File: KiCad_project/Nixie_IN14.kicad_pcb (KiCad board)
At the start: 2 copper layers, 319.8 x 69.7 mm, 65 parts, among them J1 Conn_01x10_Pin, J2 Conn_01x07_Pin, J3 Conn_01x07_Pin, J4 Conn_01x10_Pin, J5 Conn_01x07_Pin, J6 Conn_01x07_Pin, J7 USB_C_Receptacle_PowerOnly_6P, Q1 IRF540N, Q2 MMBTA42, U1 BME280_module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

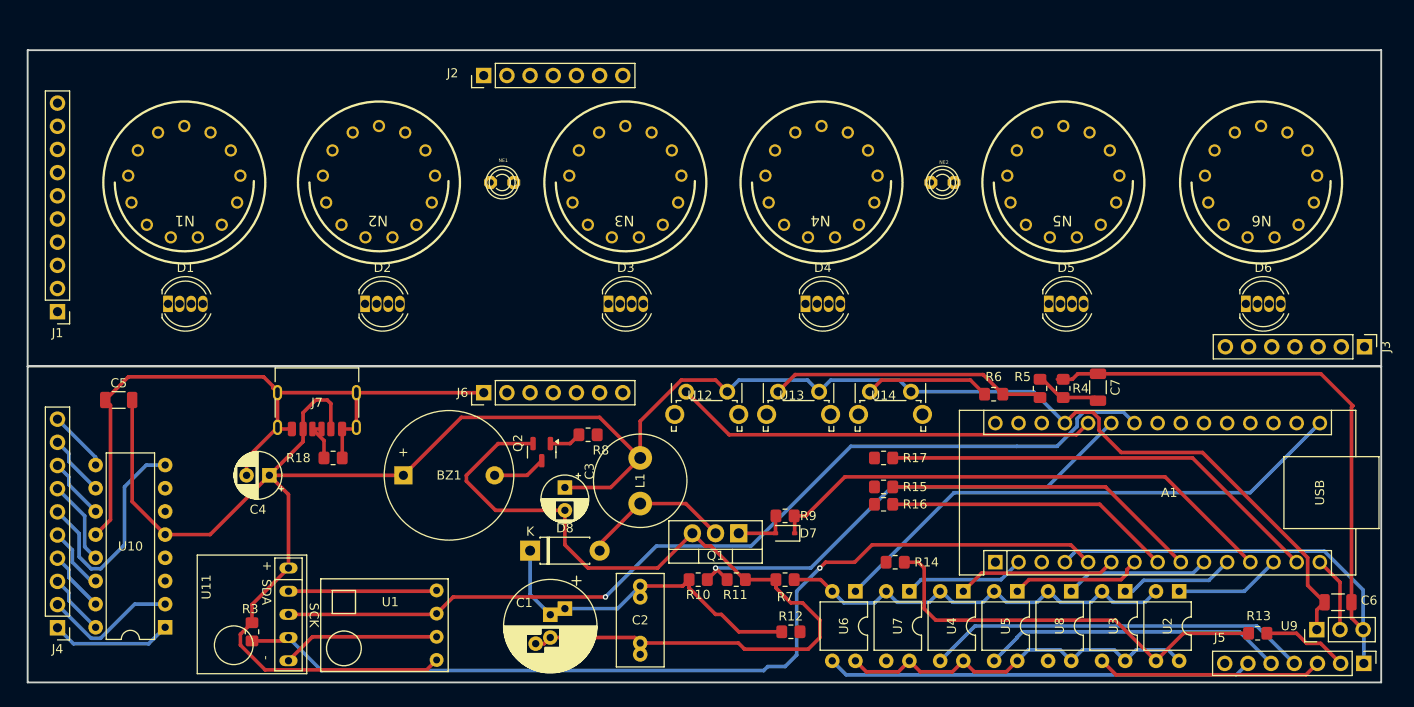
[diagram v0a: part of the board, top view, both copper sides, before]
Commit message: placeng update first version of tracing is finished
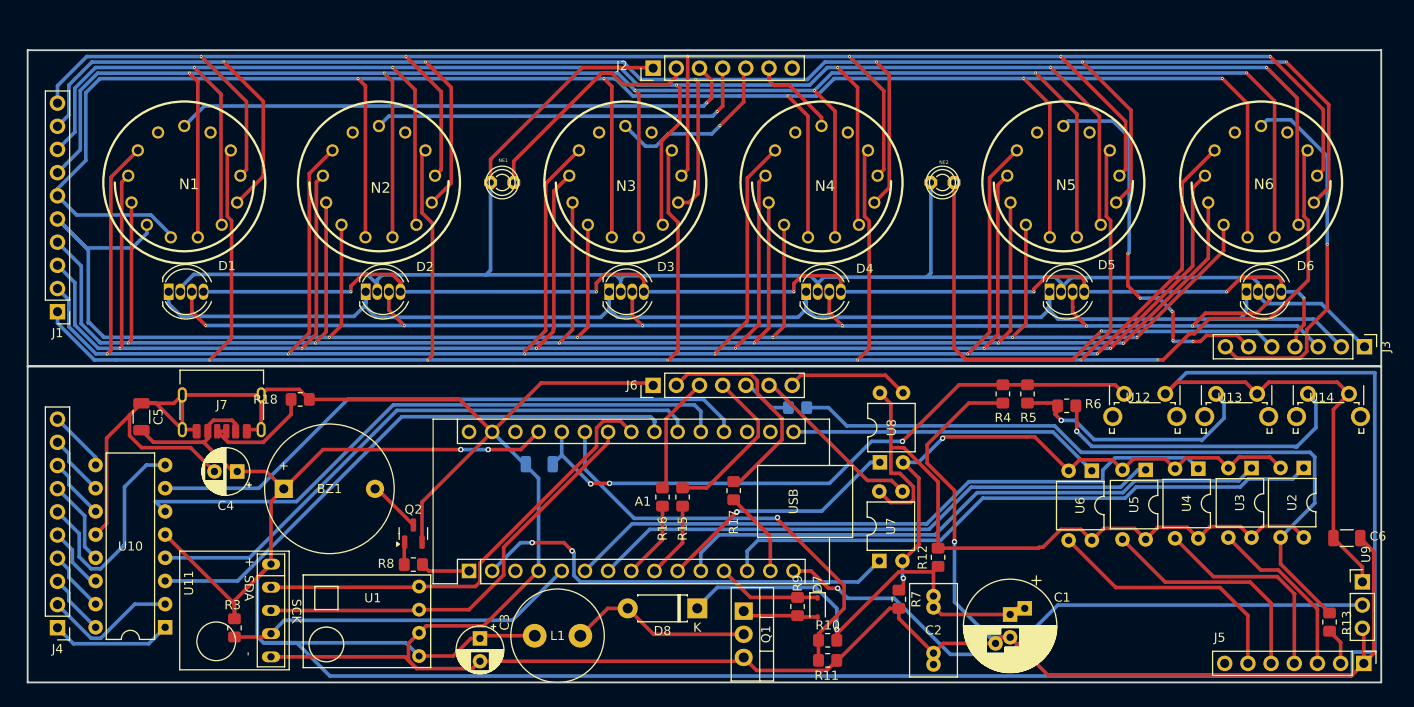
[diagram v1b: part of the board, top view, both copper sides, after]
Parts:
- C7, R14: moved to B.Cu
- moved C7 61.8 mm to (75.3, 95.3), turned to 180 degrees
- moved A1 57.7 mm to (67.6, 107.0)
- moved C1 50.4 mm to (126.9, 111.8)
- moved U12 48.0 mm to (140.9, 88.5)
- moved U13 48.0 mm to (151.0, 88.5)
- moved U14 48.0 mm to (161.0, 88.5)
- moved C2 32.2 mm to (118.5, 109.8)
- moved U6 29.1 mm to (135.8, 96.0)
- moved U4 29.0 mm to (147.5, 95.8)
- moved U8 25.3 mm to (112.6, 95.1), turned to 90 degrees
- moved R16 24.2 mm to (88.8, 98.9), turned to 90 degrees
- moved R8 23.9 mm to (61.5, 106.3)
- moved L1 22.7 mm to (74.8, 114.1), turned to 0 degrees
- moved R15 22.1 mm to (91.0, 98.9), turned to 90 degrees
- moved R14 20.0 mm to (103.6, 89.1)
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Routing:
- net Net-(J1-Pin_1): track 0.00 -> 278.9 mm, vias 0 -> 6
- net Net-(J1-Pin_2): track 0.00 -> 268.5 mm, vias 0 -> 6
- net Net-(J1-Pin_8): track 0.00 -> 250.2 mm, vias 0 -> 6
- net Net-(J1-Pin_7): track 0.00 -> 249.4 mm, vias 0 -> 6
- net Net-(J1-Pin_3): track 0.00 -> 245.2 mm, vias 0 -> 6
- net Net-(J1-Pin_9): track 0.00 -> 245.0 mm, vias 0 -> 6
- net Net-(J1-Pin_6): track 0.00 -> 242.8 mm, vias 0 -> 5
- net Net-(J1-Pin_10): track 0.00 -> 226.7 mm, vias 0 -> 6
- net Net-(J1-Pin_4): track 0.00 -> 223.7 mm, vias 0 -> 6
- net Net-(J1-Pin_5): track 0.00 -> 208.8 mm, vias 0 -> 5
- net GND: track 0.00 -> 189.4 mm
- net LED_G_top: track 0.00 -> 155.1 mm, vias 0 -> 6
- net LED_R_top: track 0.00 -> 150.9 mm
- net LED_B_top: track 0.00 -> 139.6 mm, vias 0 -> 6
- net +5V: track 244.7 -> 350.2 mm, vias 0 -> 2
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
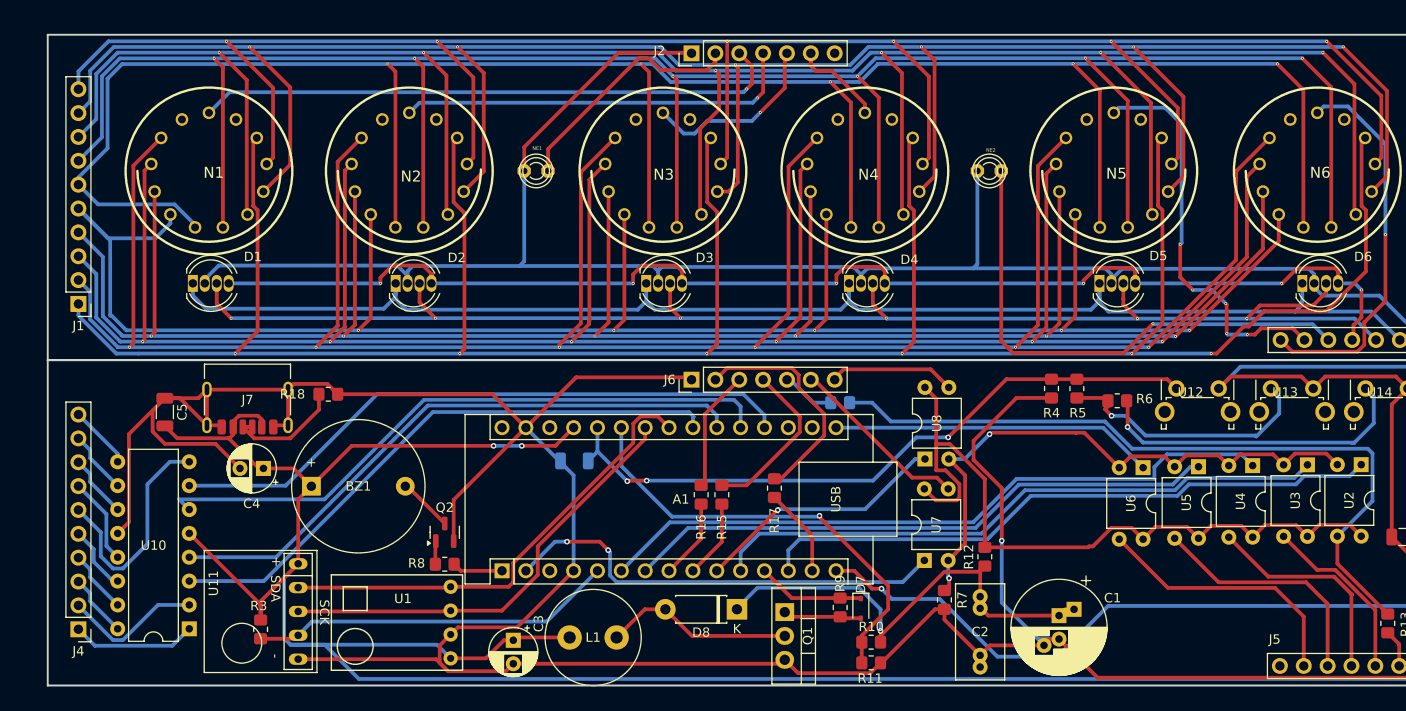
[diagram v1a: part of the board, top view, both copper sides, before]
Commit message: optimized routing and placement
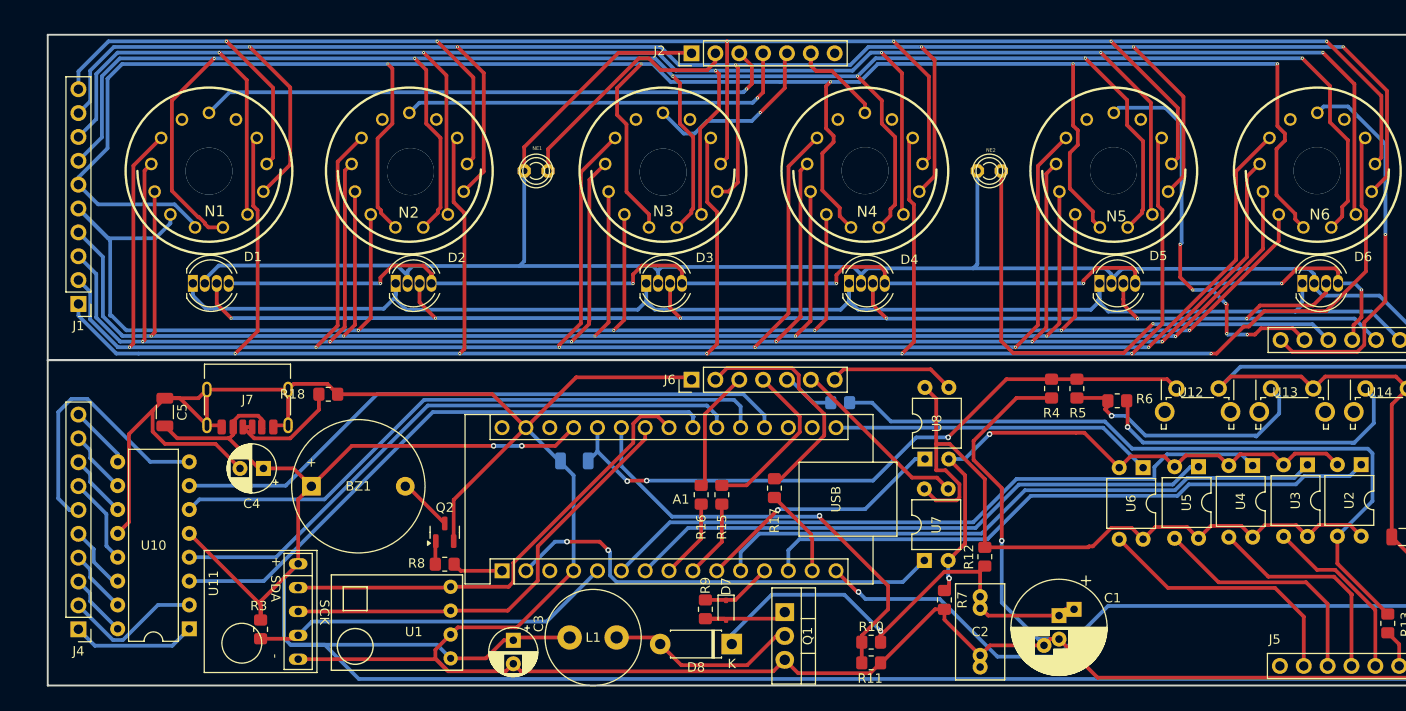
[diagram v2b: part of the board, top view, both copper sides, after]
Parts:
- moved D7 14.4 mm to (91.5, 111.2)
- moved R9 14.4 mm to (89.2, 111.1)
- moved D8 3.74 mm to (92.1, 114.8)
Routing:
- net Net-(J1-Pin_7): track 249.4 -> 261.3 mm
- net Net-(J1-Pin_6): track 242.8 -> 249.1 mm
- net 2: track 24.3 -> 29.3 mm
- net PWM_PWR: track 11.5 -> 7.57 mm
- net Net-(D7-A): track 8.37 -> 11.0 mm
- net A1_DECR: track 68.2 -> 66.1 mm
- net GNDREF: track 345.1 -> 346.1 mm
- net Net-(D8-K): track 49.7 -> 50.3 mm
- net (no net): vias 497 -> 503

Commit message: optimized placement and routing
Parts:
- moved R12 6.26 mm to (125.2, 106.2)
- moved U7 5.72 mm to (112.6, 111.6)
- moved R7 4.71 mm to (114.9, 114.8)
- moved C2 3.55 mm to (122.0, 109.7)
- moved C1 3.24 mm to (130.1, 112.3)
- moved L1 0.31 mm to (74.8, 113.8)
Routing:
- net +5V: track 350.2 -> 245.6 mm, vias 2 -> 3
- net Net-(J1-Pin_2): track 268.5 -> 194.7 mm
- net Net-(J1-Pin_1): track 278.9 -> 214.1 mm, vias 6 -> 2
- net Net-(J1-Pin_6): track 249.1 -> 213.1 mm
- net Net-(J1-Pin_3): track 245.2 -> 210.9 mm
- net Net-(J1-Pin_7): track 261.3 -> 227.8 mm
- net Net-(J1-Pin_5): track 208.8 -> 222.8 mm, vias 5 -> 7
- net Net-(J1-Pin_10): track 226.7 -> 217.4 mm
- net Net-(J1-Pin_8): track 250.2 -> 242.7 mm, vias 6 -> 7
- net LED_G_top: track 155.1 -> 148.3 mm
- net HIGH_VOLTAGE: track 77.7 -> 83.3 mm, vias 0 -> 1
- net Net-(J1-Pin_4): track 223.7 -> 228.8 mm, vias 6 -> 7
- net Net-(J1-Pin_9): track 245.0 -> 249.9 mm
- net A5: track 19.4 -> 23.6 mm
- net A1_top: track 62.9 -> 59.1 mm
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- added copper zone on B.Cu, net GND
- added copper zone on F.Cu, net GND
- added copper zone on B.Cu, net GNDREF
- added copper zone on F.Cu, net GNDREF
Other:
- board size 319.8 x 69.7 mm -> 328.6 x 72.4 mm

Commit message: increased via diameters for drilling, routing optimization
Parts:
- moved C5 48.1 mm to (79.3, 96.8), turned to 0 degrees
- moved D2 47.2 mm to (103.1, 82.1)
- moved D1 47.2 mm to (81.5, 82.1)
- moved D3 47.2 mm to (129.8, 82.1)
- moved D4 47.2 mm to (151.4, 82.1)
- moved D5 47.2 mm to (178.0, 82.1)
- moved D6 47.2 mm to (199.6, 82.1)
- moved A1 47.1 mm to (114.4, 112.3)
- moved BZ1 47.1 mm to (94.1, 103.3)
- moved C1 47.1 mm to (176.9, 117.6)
- moved C2 47.1 mm to (168.9, 114.9)
- moved C3 47.1 mm to (115.6, 119.7)
- moved C7 47.1 mm to (122.1, 100.6)
- moved D8 47.1 mm to (138.9, 120.1)
- moved J2 47.1 mm to (134.6, 57.2)
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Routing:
- net (no net): track 7090.0 -> 0.00 mm, vias 503 -> 6
- net Net-(J1-Pin_4): track 228.8 -> 211.5 mm, vias 7 -> 6
- net SDA: track 49.9 -> 62.8 mm
- net Net-(J1-Pin_5): track 222.8 -> 211.5 mm
- net LED_G_top: track 148.3 -> 140.2 mm
- net LED_R_top: track 150.9 -> 143.3 mm
- net A6_top: track 41.7 -> 35.3 mm, vias 1 -> 0
- net Net-(J1-Pin_1): track 214.1 -> 208.1 mm
- net Net-(J1-Pin_6): track 213.1 -> 218.5 mm, vias 5 -> 6
- net Net-(J1-Pin_2): track 194.7 -> 189.5 mm
- net Net-(J1-Pin_10): track 217.4 -> 212.4 mm
- net +5V: track 245.6 -> 240.7 mm
- net Net-(J1-Pin_8): track 242.7 -> 238.2 mm
- net A5: track 23.6 -> 28.2 mm
- net SQW: track 38.9 -> 42.8 mm
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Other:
- board size 328.6 x 72.4 mm -> 148.3 x 69.3 mm

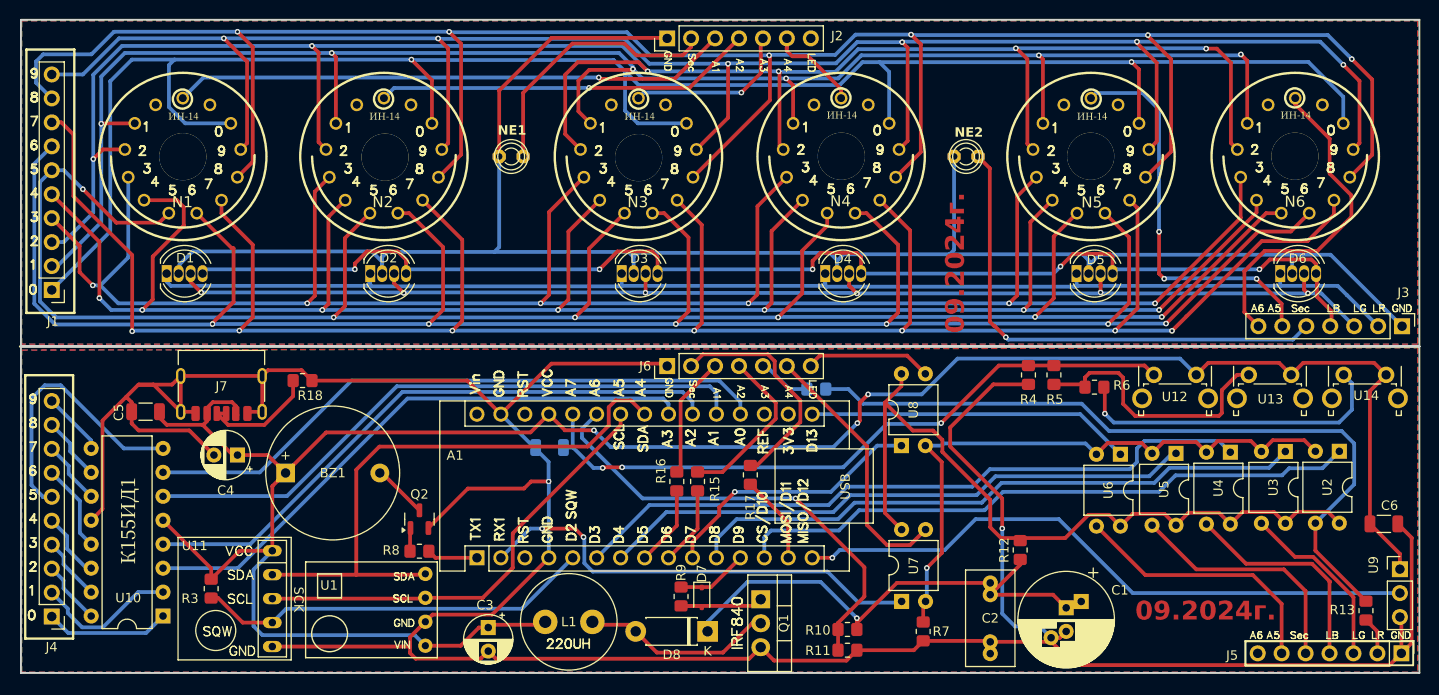
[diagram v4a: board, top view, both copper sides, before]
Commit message: added 3d models
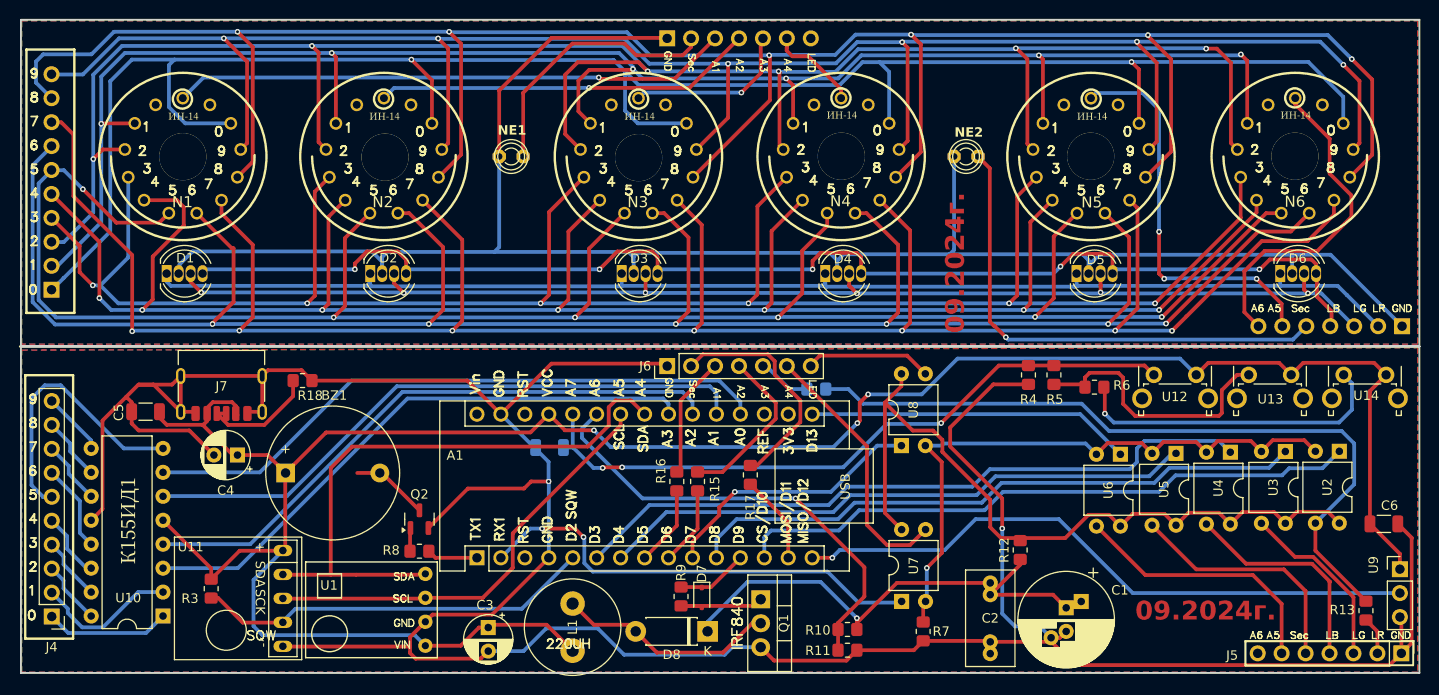
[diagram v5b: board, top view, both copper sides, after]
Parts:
- J1: footprint Connector_PinHeader_2.54mm:PinHeader_1x10_P2.54mm_Vertical -> Connector_PinSocket_2.54mm:PinSocket_1x10_P2.54mm_Vertical; moved to B.Cu
- J2, J3: footprint Connector_PinHeader_2.54mm:PinHeader_1x07_P2.54mm_Vertical -> Connector_PinSocket_2.54mm:PinSocket_1x07_P2.54mm_Vertical; moved to B.Cu
- moved L1 4.22 mm to (124.6, 122.1), turned to 90 degrees
- moved U11 1.12 mm to (93.9, 116.6)
- turned J1 to 0 degrees
- turned J2 to -90 degrees
- turned J3 to 90 degrees
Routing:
- net +5V: track 240.7 -> 245.9 mm
- net Net-(D8-A): track 20.5 -> 23.7 mm
- net Net-(BZ1--): track 5.84 -> 8.24 mm
- net SDA: track 62.8 -> 64.5 mm
- net SCL: track 47.9 -> 46.8 mm
- net GNDREF: track 342.5 -> 343.0 mm
